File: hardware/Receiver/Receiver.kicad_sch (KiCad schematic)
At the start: 121 parts, among them J1 USB_C_Receptacle_USB2.0, J3 20021511-00006T4LF, J4 Conn_01x04, J6 JST_PH, Q1 2N7002, Q10 NChan, Q11 NChan, Q2 NChan, Q3 NChan, Q4 NChan, Q5 PChan, Q6 PChan, Q7 PChan, Q8 NChan, Q9 NChan, SW1 Boot, SW1 Reset, SW2 1825027-8, U1 TPS22810DRV, U2 DMG6602SVTQ, U2 TPS22810DRV, U3 AZ1117-3.3, U3 DMG6602SVTQ, U4 TLV493DA1B6HTSA2, U7 ESP32-S3-MINI-1-N8

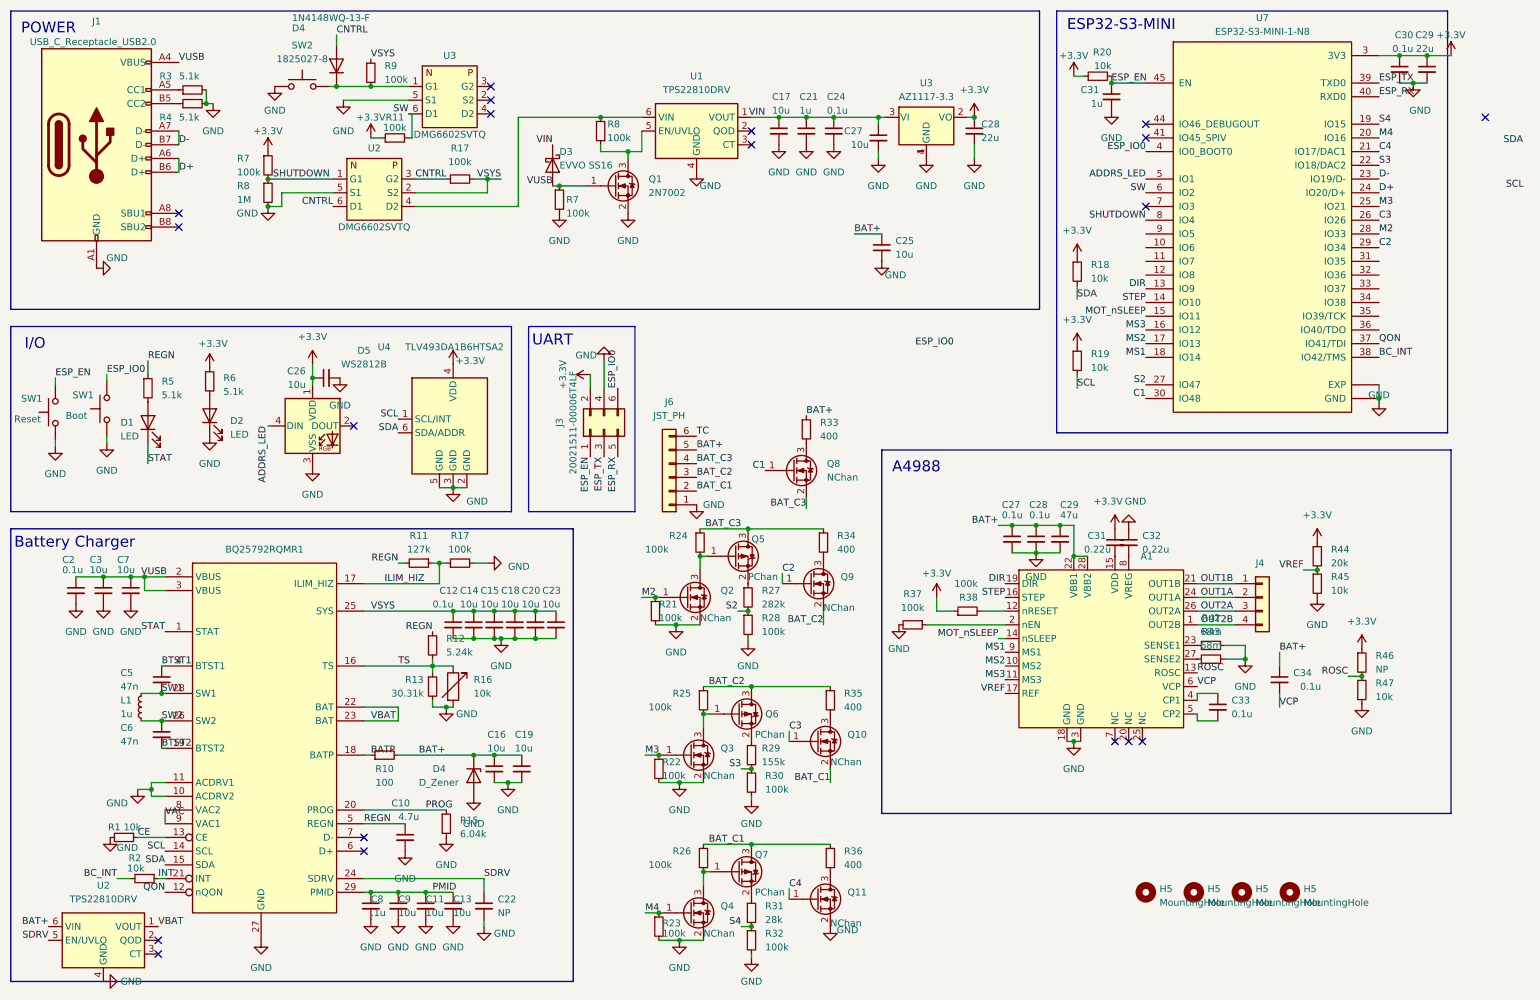
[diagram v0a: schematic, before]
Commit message: Add cell balancing
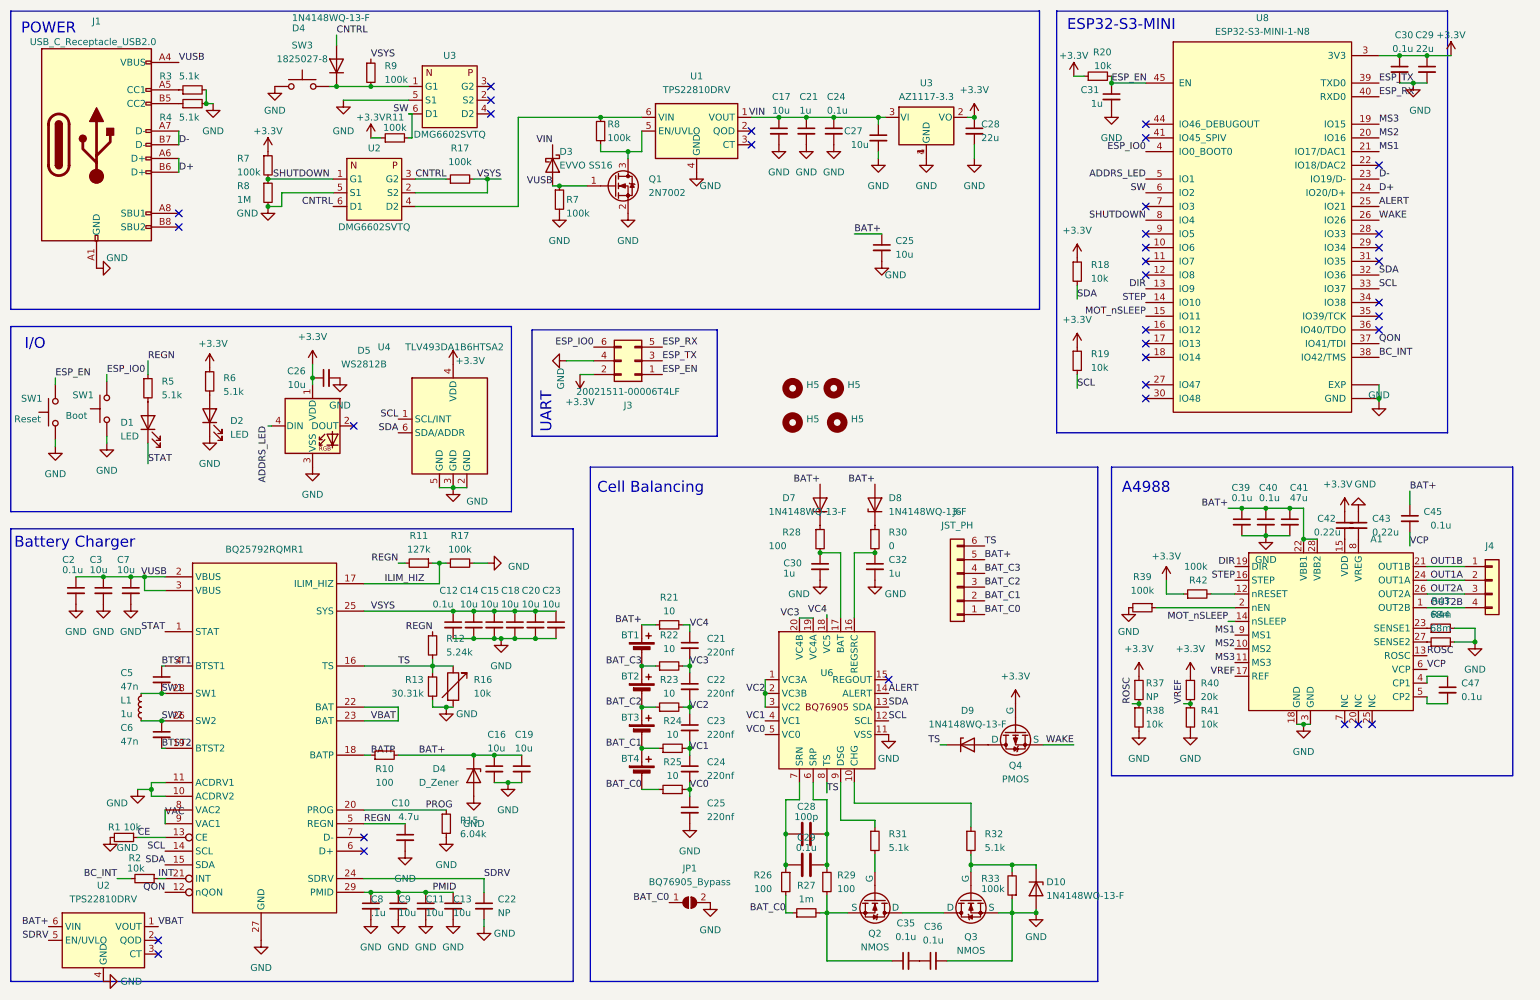
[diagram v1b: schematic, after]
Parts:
- removed Q10, Q11, Q2, Q3, Q4, Q8, Q9: NChan, Package_TO_SOT_SMD:SOT-23, symbol Transistor_FET:DMG3418L
- removed Q5, Q6, Q7: PChan, Package_TO_SOT_SMD:SOT-23, symbol Transistor_FET:BSS83P
- removed R34, R35, R36: 400, Resistor_SMD:R_2010_5025Metric, symbol Device:R_Small
- added BT1, BT2, BT3, BT4: Battery_Cell, symbol Device:Battery_Cell
- added C21, C22, C23, C24, C25: 220nf, Capacitor_SMD:C_0402_1005Metric, symbol Device:C_Small
- added C28: 100p, Capacitor_SMD:C_0402_1005Metric, symbol Device:C
- added C29: 0.1u, Capacitor_SMD:C_0402_1005Metric, symbol Device:C
- added C30, C32: 1u, Capacitor_SMD:C_0402_1005Metric, symbol Device:C_Small
- added C35, C36: 0.1u, Capacitor_SMD:C_0402_1005Metric, symbol Device:C_Small
- added D10, D7, D8, D9: 1N4148WQ-13-F, Diode_SMD:D_SOD-123, symbol Device:D_Zener
- added JP1: BQ76905_Bypass, Jumper:SolderJumper-2_P1.3mm_Open_RoundedPad1.0x1.5mm, symbol Jumper:SolderJumper_2_Open
- added Q2, Q3: NMOS, Package_TO_SOT_SMD:SOT-23, symbol Simulation_SPICE:NMOS
- added Q4: PMOS, Package_TO_SOT_SMD:SOT-23, symbol Simulation_SPICE:PMOS
- added U6: ~, Package_DFN_QFN:UQFN-20_3x3mm_P0.4mm, symbol Battery_Management_:BQ76905
- R21, R22, R23, R24, R25: value 100k -> 10
- R26, R28: value 100k -> 100
- R27: value 282k -> 1m
- R29: value 155k -> 100
- R30: value 100k -> 0
- R31: value 28k -> 5.1k
- R32: value 100k -> 5.1k
- R33: value 400 -> 100k; footprint Resistor_SMD:R_2010_5025Metric -> Resistor_SMD:R_0402_1005Metric
- renumbered C27 to C39, C28 to C40, C29 to C41, C31 to C42, C32 to C43, C34 to C45, C33 to C47, R46 to R37, R47 to R38, R37 to R39, R44 to R40, R45 to R41, R38 to R42, R42 to R43, R43 to R44, SW2 to SW3, U7 to U8
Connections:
- net C4 is gone; now on net MS1: U8.21 (IO17/DAC1)
- net TC is gone; now on net TS: J6.6 (Pin_6)
- net +3.3V: now also Q4.2 (G)
- net BAT+: now also R21.1, BT1.1 (+), D7.2 (A), D8.2 (A); no longer R33.1
- net BAT_C1: now also R24.1, BT3.2 (-), BT4.1 (+); no longer R26.1
- net BAT_C2: now also R23.1, BT2.2 (-), BT3.1 (+); no longer R25.1
- net BAT_C3: now also R22.1, BT1.2 (-), BT2.1 (+); no longer R24.1
- net GND: now also R33.1, C25.2, C30.2, C32.2, C36.2, D10.2 (A), JP1.2 (B), Q3.3 (S), U6.11 (VSS); no longer J6.1 (Pin_1), R21.2, R22.2, R23.2, R28.2, R30.2, R32.2
- net MS1: no longer U8.18 (IO14)
- net MS2: now also U8.20 (IO16); no longer U8.17 (IO13)
- net MS3: now also U8.19 (IO15); no longer U8.16 (IO12)
- net SCL: now also U8.33 (IO37), U6.12 (SCL)
- net SDA: now also U8.32 (IO36), U6.13 (SDA)
- net TS: now also D9.1 (K), U6.8 (TS)
- net BAT_C0: now reaches R26.2
- net BAT_C0: now also J6.1 (Pin_1), R25.1, R27.1, BT4.2 (-), JP1.1 (A)
- net at R29.1: now also C28.2, C29.2, U6.6 (SRP)
- net at R33.2: now also R32.2, D10.1 (K), Q3.2 (G)
- net VC0: now reaches R25.2
- net VC0: now also C24.2, C25.1, U6.5 (VC0)
- net VC1: now reaches R24.2
- net VC1: now also C23.2, C24.1, U6.4 (VC1)
- net at R31.1: now also U6.9 (DSG)
- net C1: no longer names the net of U8.30 (IO48)
- net C2: no longer names the net of U8.29 (IO34)
- net C3 renamed WAKE
- net WAKE: now also Q4.3 (S)
- net M2: no longer names the net of U8.28 (IO33)
- net M2: no longer R21.1
- net M3 renamed ALERT
- net ALERT: now also U6.14 (ALERT); no longer R22.1
- removed net M4: R23.1, U8.20 (IO16)
- removed net S2: R27.2, R28.1, U8.27 (IO47)
- removed net S3: R29.2, R30.1, U8.22 (IO18/DAC2)
- removed net S4: R31.2, R32.1, U8.19 (IO15)
- new net: C32.1, R30.2, U6.16 (REGSRC)
- new net: R32.1, U6.10 (CHG)
- new net: D9.2 (A), Q4.1 (D)
- new net: C35.1, Q2.3 (S), R27.2, R29.2
- new net: C35.2, C36.1
- new net: D8.1 (K), R30.1
- new net: Q2.1 (D), Q3.1 (D)
- new net: C28.1, C29.1, R26.1, U6.7 (SRN)
- new net: Q2.2 (G), R31.2
- new net: C30.1, R28.2, U6.17 (BAT)
- new net: D7.1 (K), R28.1
- new net VC2: C22.2, C23.1, R23.2, U6.1 (VC3A), U6.2 (VC3B), U6.3 (VC2)
- new net VC3: C21.2, C22.1, R22.2, U6.19 (VC4A), U6.20 (VC4B)
- new net VC4: C21.1, R21.2, U6.18 (VC5)
- no-connect marks 19 -> 35
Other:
- note added: "Cell Balancing"
- moved on the sheet: A1, C39, C40, C41, C42, C43, C45, C47, H5, J3, J4, J6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

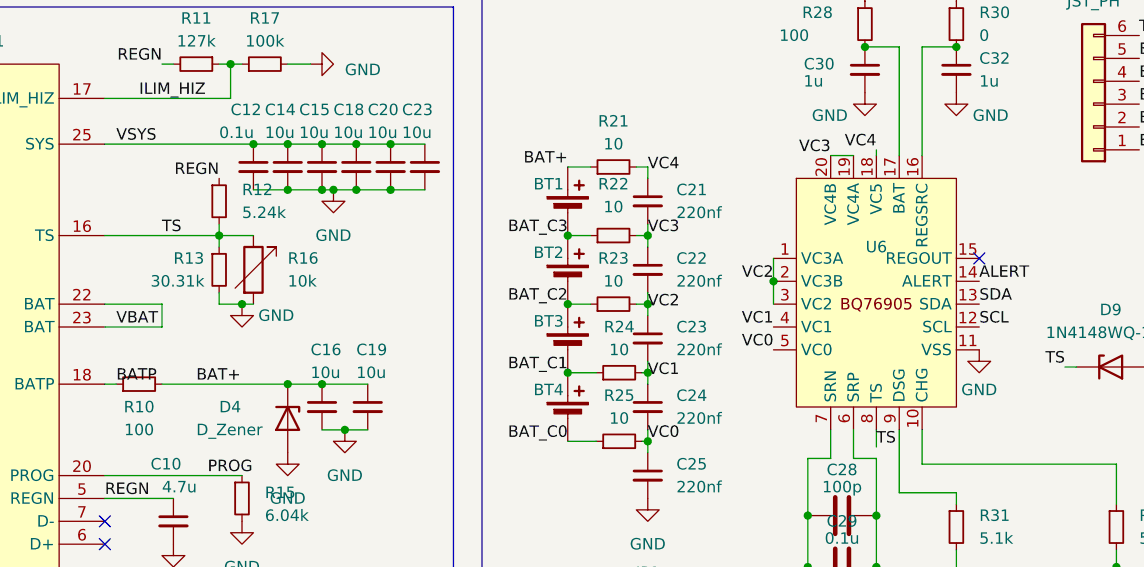
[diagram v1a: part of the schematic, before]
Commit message: add battery balancing IC
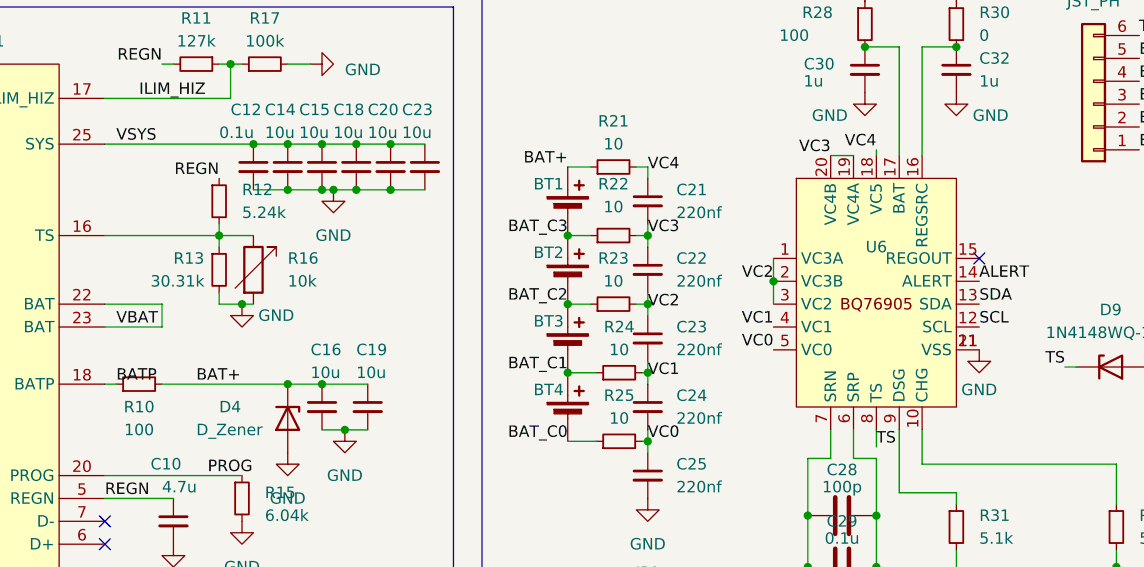
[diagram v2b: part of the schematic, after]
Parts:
- U6: footprint Package_DFN_QFN:UQFN-20_3x3mm_P0.4mm -> Package_DFN_QFN:UQFN-20-1EP_3x3mm_P0.4mm_EP1.85x1.85mm
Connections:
- net GND: now also U6.21 (VSS)
- net TS: no longer BQ25792RQMR1.16 (TS), R12.2, R13.1, R16.1
- new net: BQ25792RQMR1.16 (TS), R12.2, R13.1, R16.1
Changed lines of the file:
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@@
     (effects (font (size 1.27 1.27)) (justify left bottom))
   )
-  (label "TS" (at 86.995 136.525 0) (fields_autoplaced)
-    (effects (font (size 1.27 1.27)) (justify left bottom))
-  )
   (label "MS1" (at 241.935 130.81 180) (fields_autoplaced)
     (effects (font (size 1.27 1.27)) (justify right bottom))
@@
       (effects (font (size 1.27 1.27)))
     )
-    (property "Footprint" "Package_DFN_QFN:UQFN-20_3x3mm_P0.4mm" (at 134.62 144.145 0)
+    (property "Footprint" "Package_DFN_QFN:UQFN-20-1EP_3x3mm_P0.4mm_EP1.85x1.85mm" (at 134.62 144.145 0)
       (effects (font (size 1.27 1.27)) hide)
     )
@@
     (pin "2")
     (pin "20")
+    (pin "21")
     (pin "3")
     (pin "4")

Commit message: update readme details
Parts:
- U6: value ~ -> BQ76905
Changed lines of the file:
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@@
       (effects (font (size 1.27 1.27)))
     )
-    (property "Value" "~" (at 134.62 144.145 0)
+    (property "Value" "BQ76905" (at 134.62 144.145 0)
       (effects (font (size 1.27 1.27)))
     )
